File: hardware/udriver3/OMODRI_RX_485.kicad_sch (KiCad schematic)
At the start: 8 parts

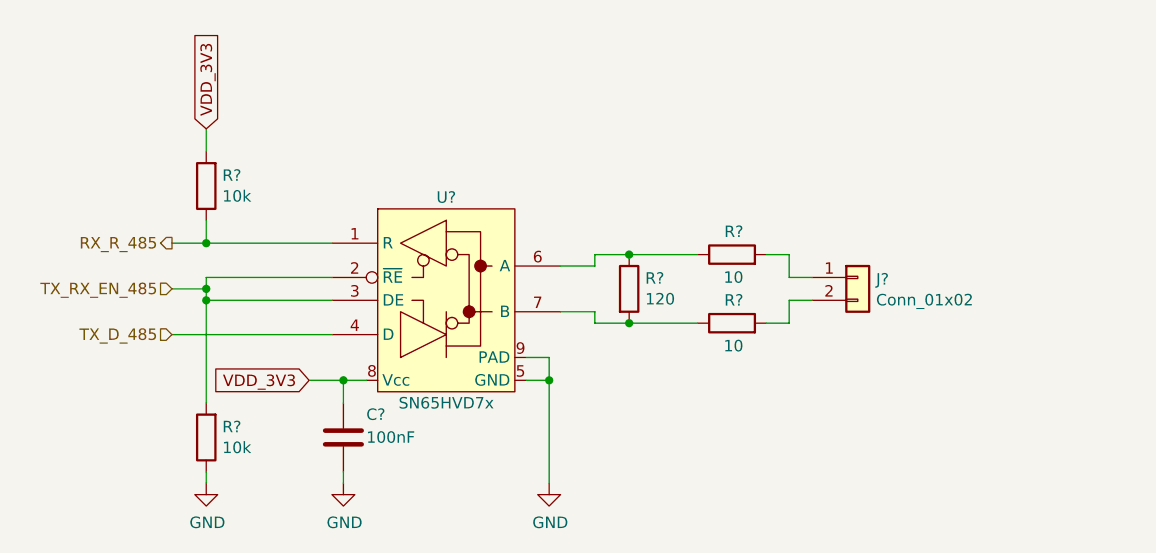
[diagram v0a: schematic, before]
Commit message: Temporary version of udrive3 v2.0. - In schematic there are 2 solutions for DC/DC buck converter. - PCB routing is not finished yet.
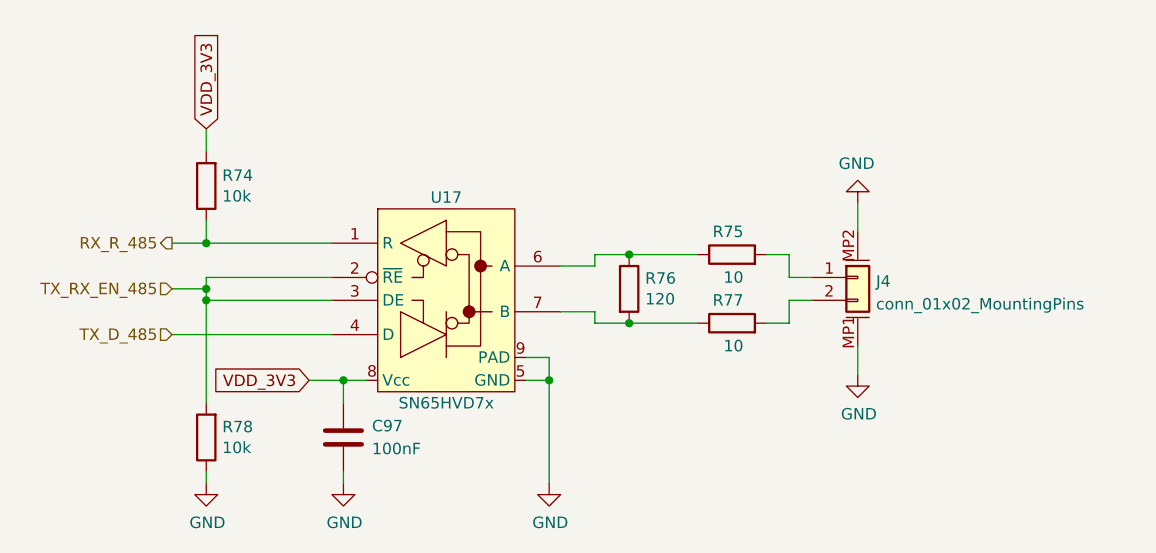
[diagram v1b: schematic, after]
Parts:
- removed J?: Conn_01x02, udriver3:DF132P125H75, symbol Connector_Generic:Conn_01x02
- added J4: conn_01x02_MountingPins, udriver3:Hirose_DF13_02P-1.25H_1x02_P1.25mm_Horizontal, symbol omodri_lib:conn_01x02_MountingPins
- R75, R77: renamed from R?; footprint Resistor_SMD:R_0603_1608Metric -> Resistor_SMD:R_0201_0603Metric; DigiKey P10.0HTR-ND -> P122669TR-ND; Farnell 2302958 -> 2302282; Mouser 667-ERJ-3EKF10R0V -> 667-ERJ-1GNF10R0C; Part No ERJ-3EKF10R0V -> ERJ-1GNF10R0C; RS 176-3533 -> 179-7137
- gave numbers to parts that had none: 5
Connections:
- net GND: now also J4.MP1 (MountPin1), J4.MP2 (MountPin2)
- net at R77.2: now also J4.2 (Pin_2)
- net at R75.2: now also J4.1 (Pin_1)
